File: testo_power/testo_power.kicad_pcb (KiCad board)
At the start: 2 copper layers, 30 x 20 mm, 6 parts, among them J1 Conn_01x06_Pin, J2 Conn_01x02_Socket, J3 Conn_01x02_Socket, Q2 FQP27P06

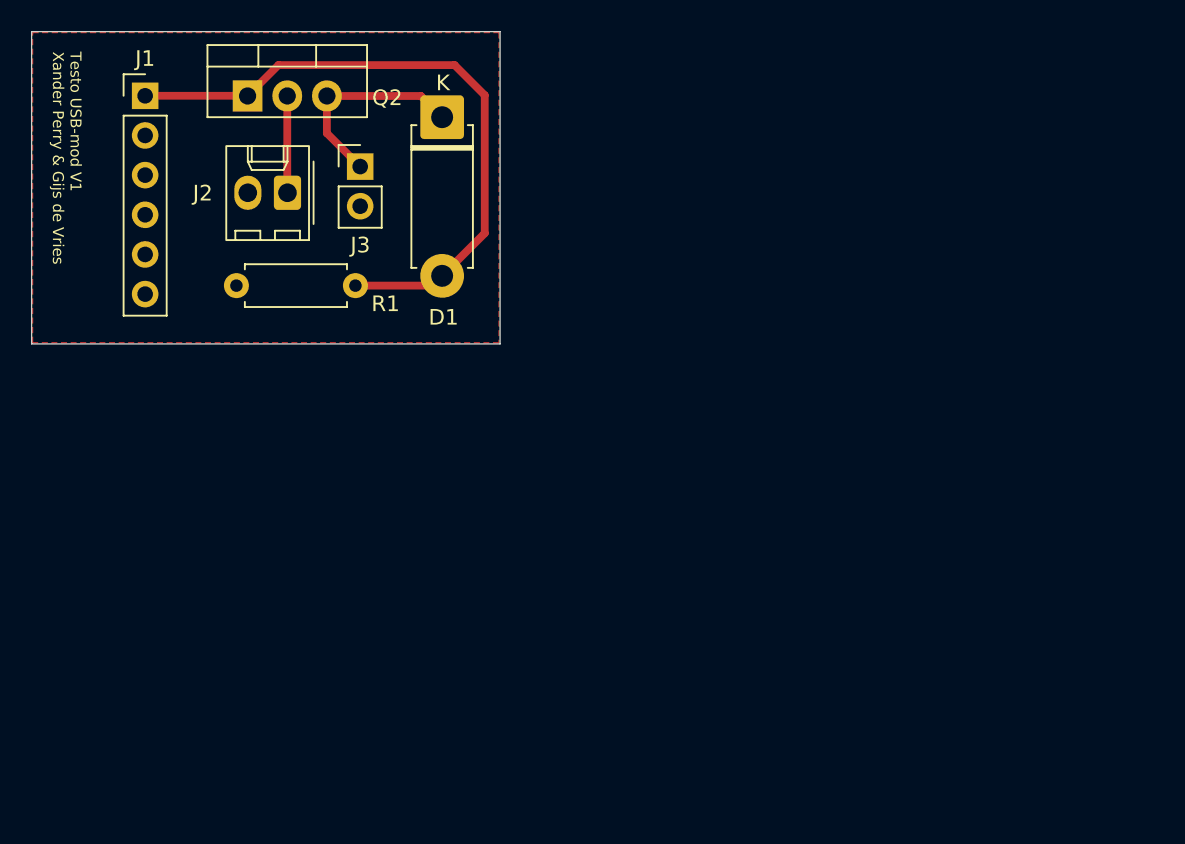
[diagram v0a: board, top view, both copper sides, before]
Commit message: Added mounting holes, added descriptions on silkscreen, added USB power indication LED.
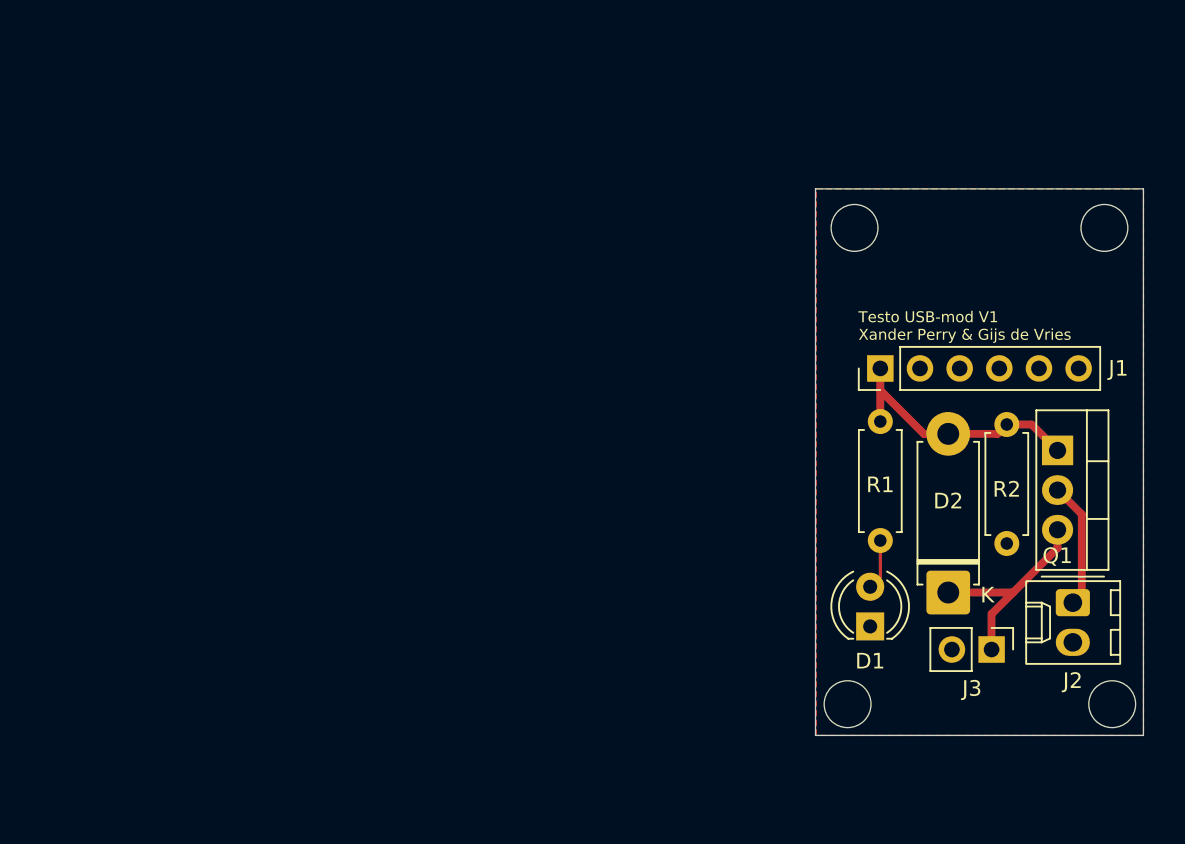
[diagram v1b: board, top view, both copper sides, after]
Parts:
- removed Q2: FQP27P06, Package_TO_SOT_THT:TO-220-3_Vertical
- added D2: D_Schottky, Diode_THT:D_5W_P10.16mm_Horizontal, F.Cu at (138.7, 115.9)
- added Q1: FQP27P06, Package_TO_SOT_THT:TO-220-3_Vertical, F.Cu at (145.7, 106.8)
- added R2: 10k, Resistor_THT:R_Axial_DIN0207_L6.3mm_D2.5mm_P7.62mm_Horizontal, F.Cu at (142.4, 105.2)
- D1: value D_Schottky -> LED GRN; footprint Diode_THT:D_5W_P10.16mm_Horizontal -> LED_THT:LED_D4.0mm
- R1: value 10k -> 150
- moved J2 56.7 mm to (146.7, 116.6), turned to -90 degrees
- moved J3 50.9 mm to (141.5, 119.6), turned to -90 degrees
- moved J1 50.2 mm to (134.3, 101.6), turned to 90 degrees
- moved D1 42.6 mm to (133.7, 118.1), turned to 90 degrees
- moved R1 34.7 mm to (134.3, 105.0), turned to -90 degrees
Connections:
- D1 pad 1: V_OUT -> GND
- D1 pad 2: V_USB -> Net-(D1-A)
- R1 pad 2: GND -> Net-(D1-A)
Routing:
- net V_USB: track 41.9 -> 16.8 mm
- net Net-(D1-A): track 0.00 -> 3.23 mm
- net V_BAT: track 6.37 -> 8.09 mm
- net V_OUT: track 13.4 -> 13.9 mm
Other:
- board size 30 x 20 mm -> 21 x 35 mm
- board text added: "USB-C breakout board"

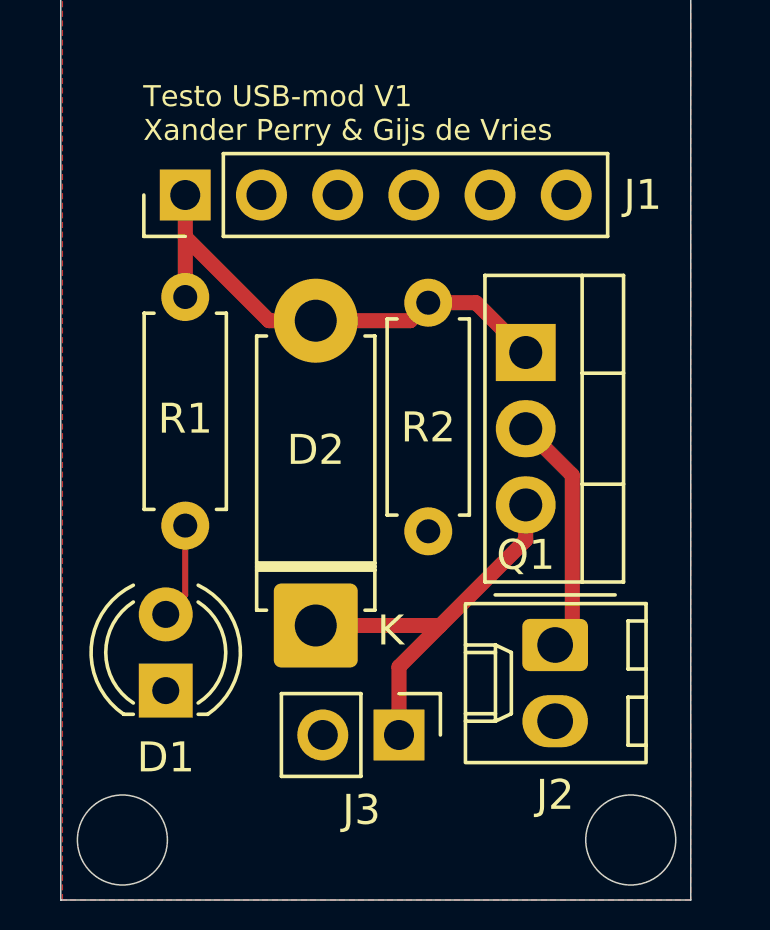
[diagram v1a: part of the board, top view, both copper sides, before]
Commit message: made traces 1mm thick
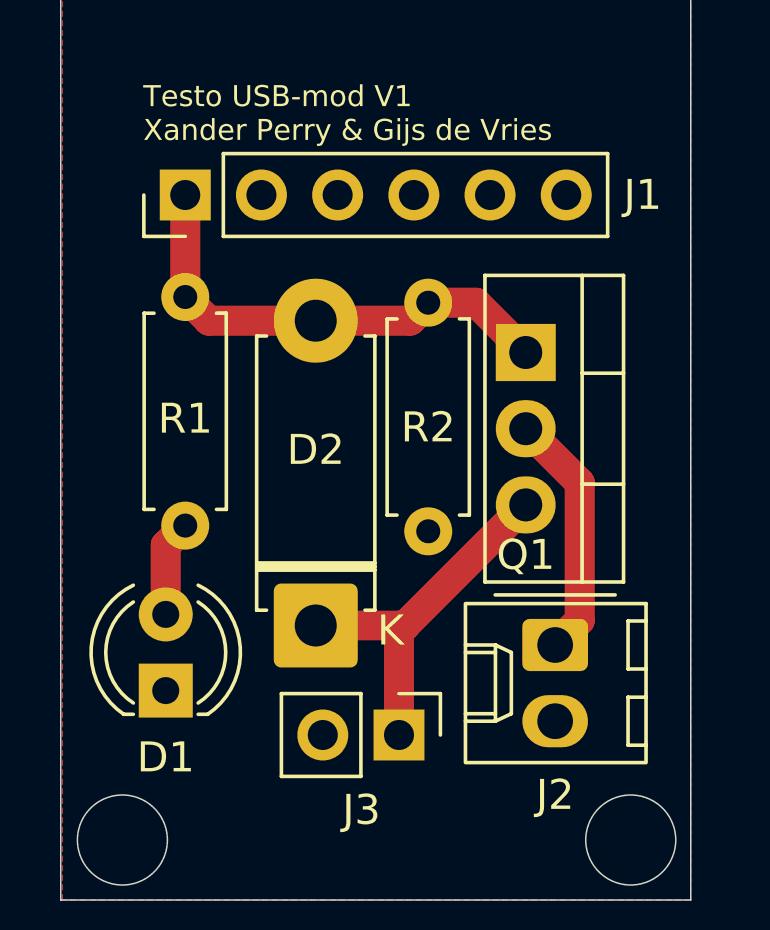
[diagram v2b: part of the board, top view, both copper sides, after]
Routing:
- net V_OUT: track 13.9 -> 12.8 mm
- net V_BAT: track 8.09 -> 9.10 mm
- net V_USB: track 16.8 -> 16.0 mm
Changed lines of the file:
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@@
 	)
 	(segment
-		(start 142.85 115.92)
-		(end 138.7 115.92)
+		(start 133.7 115.55)
+		(end 133.7 113.24)
+		(width 1)
+		(layer "F.Cu")
+		(net "Net-(D1-A)")
+	)
+	(segment
+		(start 133.7 113.24)
+		(end 134.35 112.59)
+		(width 1)
+		(layer "F.Cu")
+		(net "Net-(D1-A)")
+	)
+	(segment
+		(start 145.7 109.36)
+		(end 147.5 111.16)
+		(width 1)
+		(layer "F.Cu")
+		(net "V_BAT")
+	)
+	(segment
+		(start 147.25 116)
+		(end 146.68 116.57)
 		(width 0.5)
 		(layer "F.Cu")
-		(net "V_OUT")
+		(net "V_BAT")
 	)
 	(segment
-		(start 145.7 113.07)
-		(end 142.85 115.92)
-		(width 0.5)
+		(start 147.5 115.75)
+		(end 146.68 116.57)
+		(width 1)
 		(layer "F.Cu")
-		(net "V_OUT")
+		(net "V_BAT")
 	)
 	(segment
-		(start 145.7 111.899999)
-		(end 145.7 113.07)
-		(width 0.5)
+		(start 147.5 111.16)
+		(end 147.5 115.75)
+		(width 1)
+		(layer "F.Cu")
+		(net "V_BAT")
+	)
+	(segment
+		(start 135.14 105.76)
+		(end 134.35 104.97)
+		(width 1)
+		(layer "F.Cu")
+		(net "V_USB")
+	)
+	(segment
+		(start 142.45 105.16)
+		(end 144.04 105.16)
+		(width 1)
+		(layer "F.Cu")
+		(net "V_USB")
+	)
+	(segment
+		(start 138.7 105.76)
+		(end 141.85 105.76)
+		(width 1)
+		(layer "F.Cu")
+		(net "V_USB")
+	)
+	(segment
+		(start 134.35 104.97)
+		(end 134.35 101.57)
+		(width 1)
+		(layer "F.Cu")
+		(net "V_USB")
+	)
+	(segment
+		(start 144.04 105.16)
+		(end 145.7 106.82)
+		(width 1)
+		(layer "F.Cu")
+		(net "V_USB")
+	)
+	(segment
+		(start 141.85 105.76)
+		(end 142.45 105.16)
+		(width 1)
+		(layer "F.Cu")
+		(net "V_USB")
+	)
+	(segment
+		(start 138.7 105.76)
+		(end 135.14 105.76)
+		(width 1)
+		(layer "F.Cu")
+		(net "V_USB")
+	)
+	(segment
+		(start 141.679999 115.92)
+		(end 138.7 115.92)
+		(width 1)
 		(layer "F.Cu")
 		(net "V_OUT")
@@
 	)
 	(segment
-		(start 141.475 117.295)
-		(end 142.85 115.92)
-		(width 0.5)
+		(start 145.7 111.899999)
+		(end 141.679999 115.92)
+		(width 1)
+		(layer "F.Cu")
+		(net "V_OUT")
+	)
+	(segment
+		(start 141.475 116.124999)
+		(end 141.679999 115.92)
+		(width 1)
 		(layer "F.Cu")
 		(net "V_OUT")
@@
 	(segment
 		(start 141.475 119.57)
-		(end 141.475 117.295)
-		(width 0.5)
+		(end 141.475 116.124999)
+		(width 1)
 		(layer "F.Cu")
 		(net "V_OUT")
 	)
-	(segment
-		(start 138.7 105.76)
-		(end 141.85 105.76)
-		(width 0.5)
-		(layer "F.Cu")
-		(net "V_USB")
-	)
-	(segment
-		(start 138.7 105.76)
-		(end 137.14 105.76)
-		(width 0.5)
-		(layer "F.Cu")
-		(net "V_USB")
-	)
-	(segment
-		(start 134.35 102.97)
-		(end 134.35 101.57)
-		(width 0.5)
-		(layer "F.Cu")
-		(net "V_USB")
-	)
-	(segment
-		(start 134.35 102.97)
-		(end 134.35 104.97)
-		(width 0.5)
-		(layer "F.Cu")
-		(net "V_USB")
-	)
-	(segment
-		(start 141.85 105.76)
-		(end 142.45 105.16)
-		(width 0.5)
-		(layer "F.Cu")
-		(net "V_USB")
-	)
-	(segment
-		(start 142.45 105.16)
-		(end 144.04 105.16)
-		(width 0.5)
-		(layer "F.Cu")
-		(net "V_USB")
-	)
-	(segment
-		(start 137.14 105.76)
-		(end 134.35 102.97)
-		(width 0.5)
-		(layer "F.Cu")
-		(net "V_USB")
-	)
-	(segment
-		(start 144.04 105.16)
-		(end 145.7 106.82)
-		(width 0.5)
-		(layer "F.Cu")
-		(net "V_USB")
-	)
-	(segment
-		(start 145.7 109.36)
-		(end 147.25 110.91)
-		(width 0.5)
-		(layer "F.Cu")
-		(net "V_BAT")
-	)
-	(segment
-		(start 147.25 110.91)
-		(end 147.25 116)
-		(width 0.5)
-		(layer "F.Cu")
-		(net "V_BAT")
-	)
-	(segment
-		(start 147.25 116)
-		(end 146.68 116.57)
-		(width 0.5)
-		(layer "F.Cu")
-		(net "V_BAT")
-	)
-	(segment
-		(start 134.35 114.9)
-		(end 133.7 115.55)
-		(width 0.2)
-		(layer "F.Cu")
-		(net "Net-(D1-A)")
-	)
-	(segment
-		(start 134.35 112.59)
-		(end 134.35 114.9)
-		(width 0.2)
-		(layer "F.Cu")
-		(net "Net-(D1-A)")
-	)
 	(zone

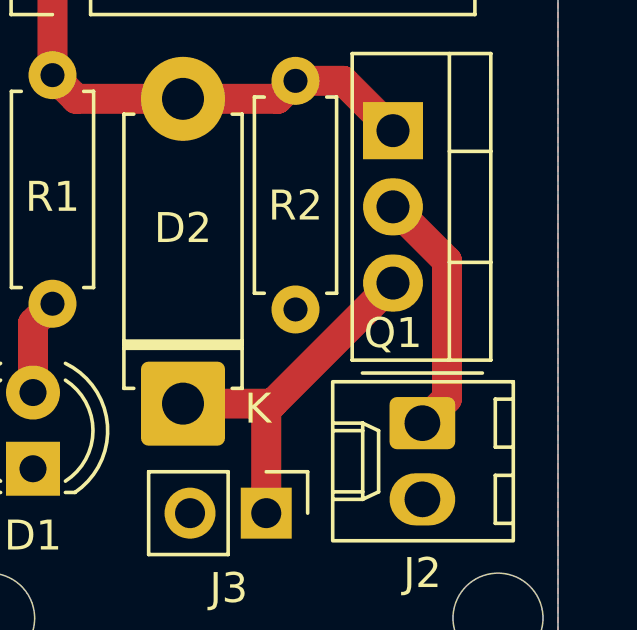
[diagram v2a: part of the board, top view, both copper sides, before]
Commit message: routed new wire
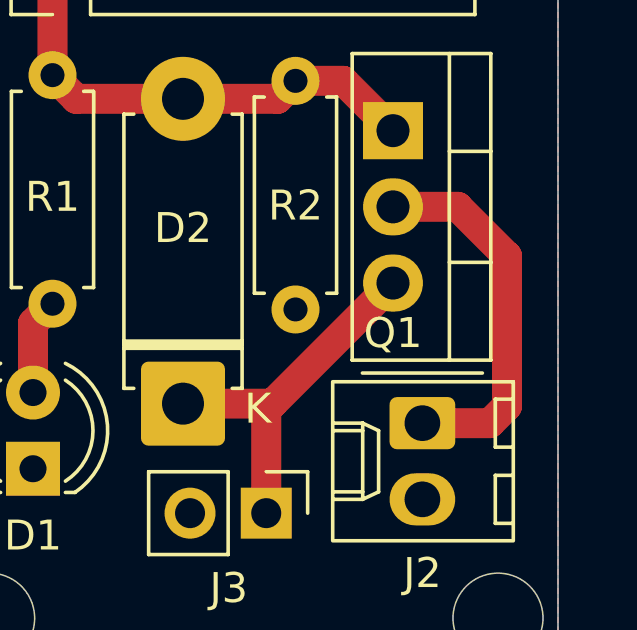
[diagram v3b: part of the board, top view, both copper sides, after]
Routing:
- net V_BAT: track 9.10 -> 12.5 mm
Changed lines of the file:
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@@
 	)
 	(segment
-		(start 145.7 109.36)
-		(end 147.5 111.16)
+		(start 147.86 109.36)
+		(end 145.7 109.36)
 		(width 1)
 		(layer "F.Cu")
@@
 	)
 	(segment
-		(start 147.25 116)
-		(end 146.68 116.57)
-		(width 0.5)
-		(layer "F.Cu")
-		(net "V_BAT")
-	)
-	(segment
-		(start 147.5 115.75)
-		(end 146.68 116.57)
+		(start 148.93 116.57)
+		(end 149.5 116)
 		(width 1)
 		(layer "F.Cu")
@@
 	)
 	(segment
-		(start 147.5 111.16)
-		(end 147.5 115.75)
+		(start 146.68 116.57)
+		(end 148.93 116.57)
 		(width 1)
 		(layer "F.Cu")
+		(net "V_BAT")
+	)
+	(segment
+		(start 149.5 116)
+		(end 149.5 111)
+		(width 1)
+		(layer "F.Cu")
+		(net "V_BAT")
+	)
+	(segment
+		(start 149.5 111)
+		(end 147.86 109.36)
+		(width 1)
+		(layer "F.Cu")

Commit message: pcb and schematic done
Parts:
- removed Q1: FQP27P06, Package_TO_SOT_THT:TO-220-3_Vertical
- added Q2: IRLML6402TRPBF, Package_TO_SOT_SMD:SOT-23, F.Cu at (108.0, 118.1)
- added R3: 150R, Resistor_SMD:R_0603_1608Metric, F.Cu at (102.5, 121.0)
- added R4: 10k, Resistor_SMD:R_0603_1608Metric, F.Cu at (102.8, 116.5)
- D1: value LED GRN -> LED RED; footprint LED_THT:LED_D4.0mm -> LED_SMD:LED_0603_1608Metric
- D2: value D_Schottky -> SS14; footprint Diode_THT:D_5W_P10.16mm_Horizontal -> Diode_SMD:D_SMA
- J1: value Conn_01x06_Pin -> USB_C_Receptacle_PowerOnly_6P; footprint Connector_PinHeader_2.54mm:PinHeader_1x06_P2.54mm_Vertical -> Connector_USB:USB_C_Receptacle_HCTL_HC-TYPE-C-16P-01A
- J2: footprint Connector_Molex:Molex_KK-254_AE-6410-02A_1x02_P2.54mm_Vertical -> Connector_Molex:Molex_CLIK-Mate_502382-0270_1x02-1MP_P1.25mm_Vertical
- J3: footprint Connector_PinHeader_2.54mm:PinHeader_1x02_P2.54mm_Vertical -> Connector_Molex:Molex_KK-254_AE-6410-02A_1x02_P2.54mm_Vertical
- R1: value 150 -> 5k1; footprint Resistor_THT:R_Axial_DIN0207_L6.3mm_D2.5mm_P7.62mm_Horizontal -> Resistor_SMD:R_0603_1608Metric
- R2: value 10k -> 5k1; footprint Resistor_THT:R_Axial_DIN0207_L6.3mm_D2.5mm_P7.62mm_Horizontal -> Resistor_SMD:R_0603_1608Metric
- moved J2 38.6 mm to (110.0, 104.5), turned to 0 degrees
- moved D2 35.5 mm to (103.5, 111.0), turned to -90 degrees
- moved J1 34.4 mm to (110.0, 125.8), turned to 0 degrees
- moved D1 31.9 mm to (102.5, 124.5)
- moved R2 29.6 mm to (118.5, 122.5), turned to 90 degrees
- moved J3 25.5 mm to (116.5, 114.2)
- moved R1 25.0 mm to (116.5, 122.5), turned to 90 degrees
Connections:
- D2 pad 2: V_USB -> V_BUS
- J2 pad 1: V_BAT -> V_OUT
- J3 pad 1: V_OUT -> V_BAT
- R1 pad 1: V_USB -> GND
- R1 pad 2: Net-(D1-A) -> Net-(J1-CC2)
- R2 pad 1: V_USB -> GND
- R2 pad 2: GND -> Net-(J1-CC1)
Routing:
- net V_BUS: track 0.00 -> 28.0 mm
- net V_USB: track 16.0 -> 0.00 mm
- net Net-(J1-CC1): track 0.00 -> 12.6 mm
- net Net-(J1-CC2): track 0.00 -> 6.49 mm
- net V_OUT: track 12.8 -> 16.9 mm
- net V_BAT: track 12.5 -> 9.58 mm
- net Net-(D1-A): track 3.23 -> 1.89 mm
- added copper zone on B.Cu, net GND
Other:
- board size 21 x 35 mm -> 20 x 30 mm
- board text added: "GND"
- board text added: "USB PWR LED"
- board text added: "V_BAT"
- board text added: "V_OUT"
- board text removed: "Testo USB-mod V1 Xander Perry & Gijs de Vries"
- board text removed: "USB-C breakout board"

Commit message: added some silkscreen
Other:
- board text added: "Power Source Selector"
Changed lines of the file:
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@@
 		(capping no)
 		(filling no)
-		(zone_defaults)
 		(pcbplotparams
 			(layerselection 0x00000000_00000000_55555555_5755f5ff)
@@
 		(layer "Edge.Cuts")
 	)
+	(gr_text "Power Source Selector"
+		(at 109 116 90)
+		(layer "F.SilkS")
+		(effects
+			(font
+				(size 0.3 0.3)
+				(thickness 0.075)
+				(bold yes)
+			)
+			(justify left bottom)
+		)
+	)
 	(gr_text "USB PWR LED"

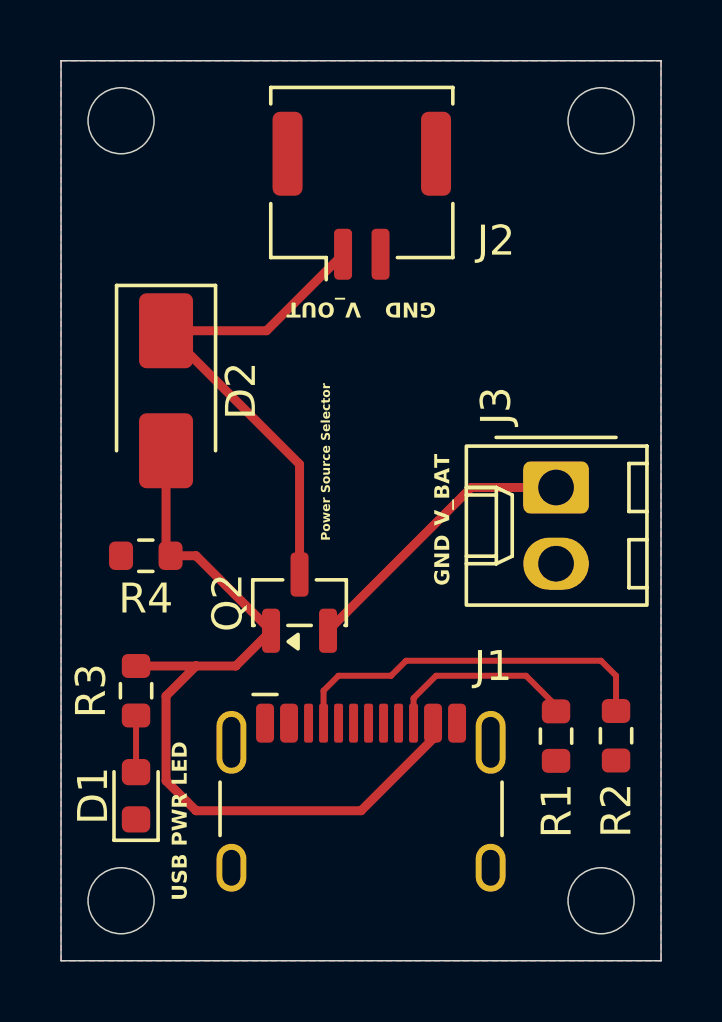
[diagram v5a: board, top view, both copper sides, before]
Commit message: replaced connectors
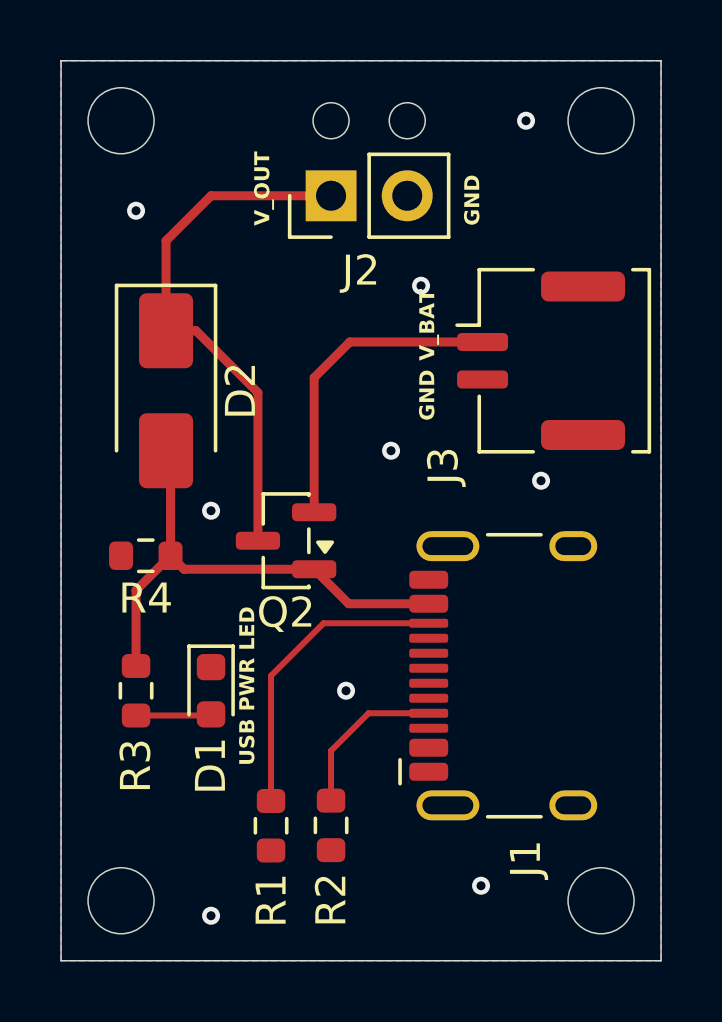
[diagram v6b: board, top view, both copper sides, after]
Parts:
- J2: footprint Connector_Molex:Molex_CLIK-Mate_502382-0270_1x02-1MP_P1.25mm_Vertical -> Connector_PinHeader_2.54mm:PinHeader_1x02_P2.54mm_Vertical
- J3: footprint Connector_Molex:Molex_KK-254_AE-6410-02A_1x02_P2.54mm_Vertical -> Connector_Molex:Molex_CLIK-Mate_502382-0270_1x02-1MP_P1.25mm_Vertical
- moved R1 9.96 mm to (107.0, 125.5)
- moved R2 9.96 mm to (109.0, 125.5)
- moved J1 8.02 mm to (116.0, 120.5), turned to 90 degrees
- moved D1 4.30 mm to (105.0, 121.0), turned to -90 degrees
- moved J3 4.25 mm to (116.0, 110.0)
- moved Q2 2.11 mm to (107.5, 116.0), turned to 180 degrees
- moved J2 1.03 mm to (109.0, 104.5), turned to 90 degrees
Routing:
- net V_BUS: track 28.0 -> 17.0 mm
- net Net-(J1-CC1): track 12.6 -> 5.44 mm
- net Net-(J1-CC2): track 6.49 -> 10.2 mm
- net V_OUT: track 16.9 -> 18.0 mm
- net V_BAT: track 9.58 -> 10.6 mm
- net Net-(D1-A): track 1.89 -> 2.52 mm
- net GND: vias 0 -> 9
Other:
- outline, holes or cut-outs redrawn
- board text removed: "Power Source Selector"
